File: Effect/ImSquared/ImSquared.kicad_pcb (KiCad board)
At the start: 2 copper layers, 32 x 68.5 mm, 32 parts, among them J1 Conn_01x04_Pin, J2 Conn_01x03_Pin, Q1 DMMT5551, Q2 DMMT5551, Q3 DMMT5551, Q4 DMMT5551, U1 OPA1656, U2 OPA1656

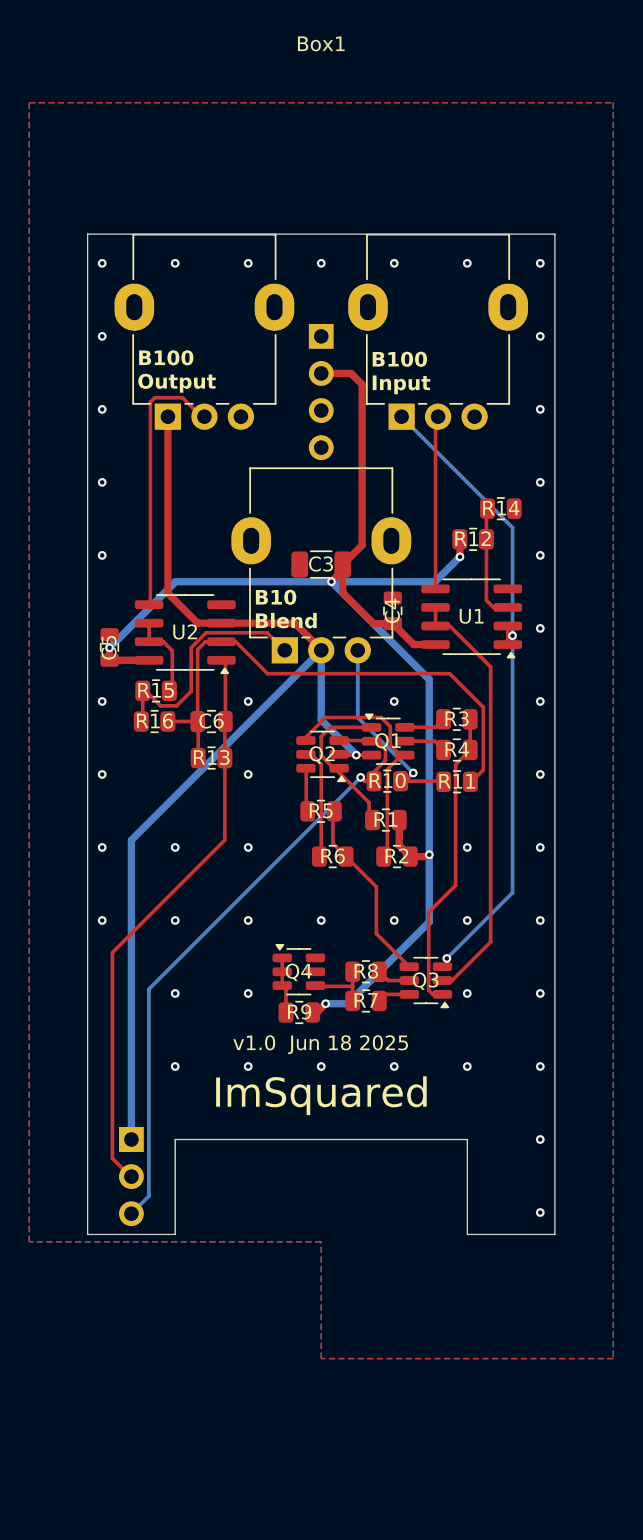
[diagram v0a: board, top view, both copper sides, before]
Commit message: ImSquared: fix enormously stupid mistake
Capacitors C1/C2 had been marked "Exclude from board", because they were
copied from a test capacitor I had in a sim-only circuit.  And I didn't
notice at any point that the PCB design didn't have them.

Not even when populating the board.  I did notice that the components on
the BOM started from C3, and I just idly thought - without looking any
closer at it - that I had forgotten to re-annotate the circuit.

So I never gave it another thought - until none of the signal actually
made it to the analog multiplier unit, so the board didn't actually work
at all.  D'oh!

Trivial fix, but oh how annoying.  KiCad makes it visually clear when a
component is excluded from simulation, and when a component is marked
"Do not populate".  But something marked "Exclude from board" is clearly
too easy to miss.  I need to be more careful.

I was able to bodge-wire this, with three of four endpoints of the two
mislaid caps being through-hole (the 'IN' signal source, and two
potentiometer pins).  For the fourth signal ('OUT1') I just soldered a
wire to the 2.2kOhm resistor.

I _hate_ soldering wire and my bodge wires weren't pretty.  But the
alternative was "wait a week for fixed boards to test because you're a
dum-dum".

The circuit does actually work and seems to behave exactly like in
simulation.  Lovely.

Signed-off-by: Linus Torvalds <torvalds@linux-foundation.org>
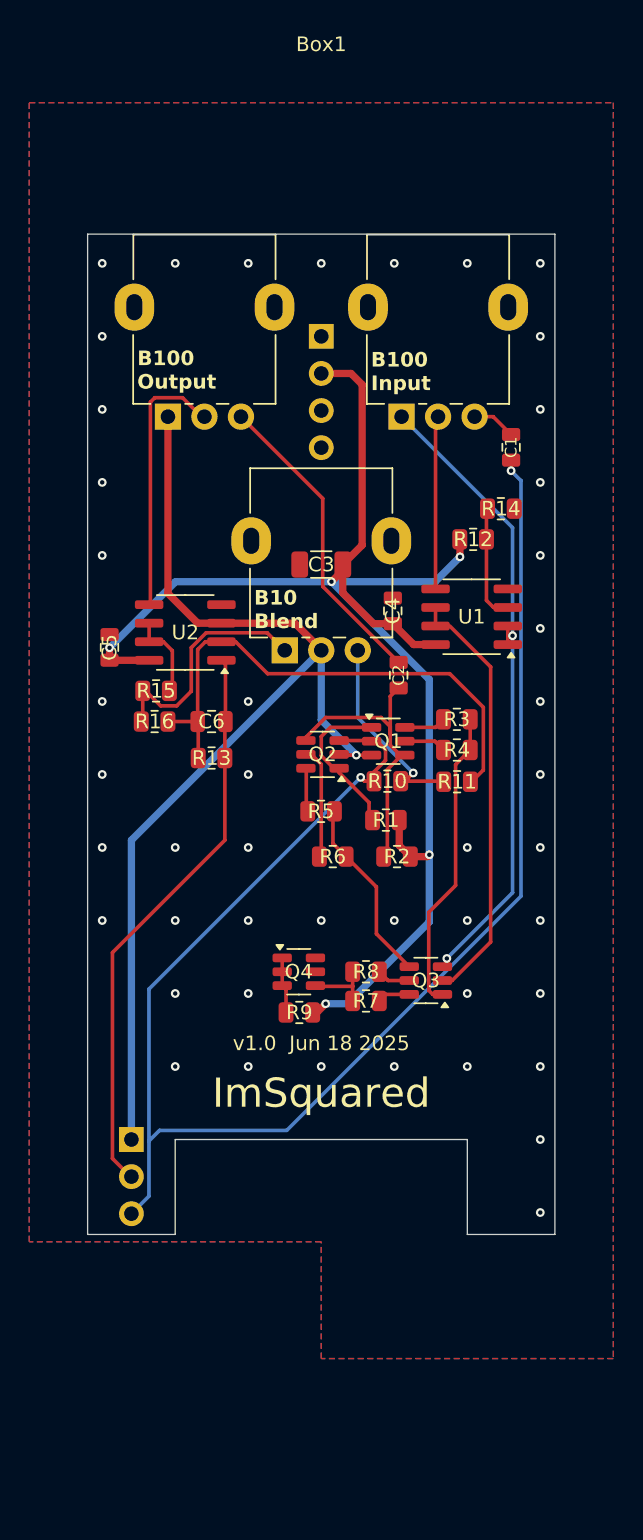
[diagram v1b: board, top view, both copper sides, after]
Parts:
- added C1: 0.1uF, Mylib:C_0704_1810Metric, F.Cu at (113.0, 77.6)
- added C2: 0.1uF, Mylib:C_0704_1810Metric, F.Cu at (105.3, 93.2)
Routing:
- net IN: track 42.9 -> 105.4 mm, vias 1 -> 2
- net Net-(C2-Pad2): track 0.00 -> 21.3 mm
- net OUT1: track 16.2 -> 19.5 mm
- net Net-(C1-Pad2): track 0.00 -> 3.01 mm
- net GND: vias 47 -> 46
